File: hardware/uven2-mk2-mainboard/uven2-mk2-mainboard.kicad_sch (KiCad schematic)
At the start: 126 parts, among them J1 LEDs, J10 GND, J11 24V, J12 GND, J13 24V, J14 GND, J15 Chamber_Control, J17 PowerON/OFF, J2 1-282834-0, J3 5V, J4 GND, J5 J1B1211CCD, J6 24V, J7 GND, J8 USB_HOST, J9 24V, Q1 2N7002, Q2 2N7002, U1 DEV-16771, U2 MCP48FEB28T-20E/ST, U3 MCP48FEB28T-20E/ST

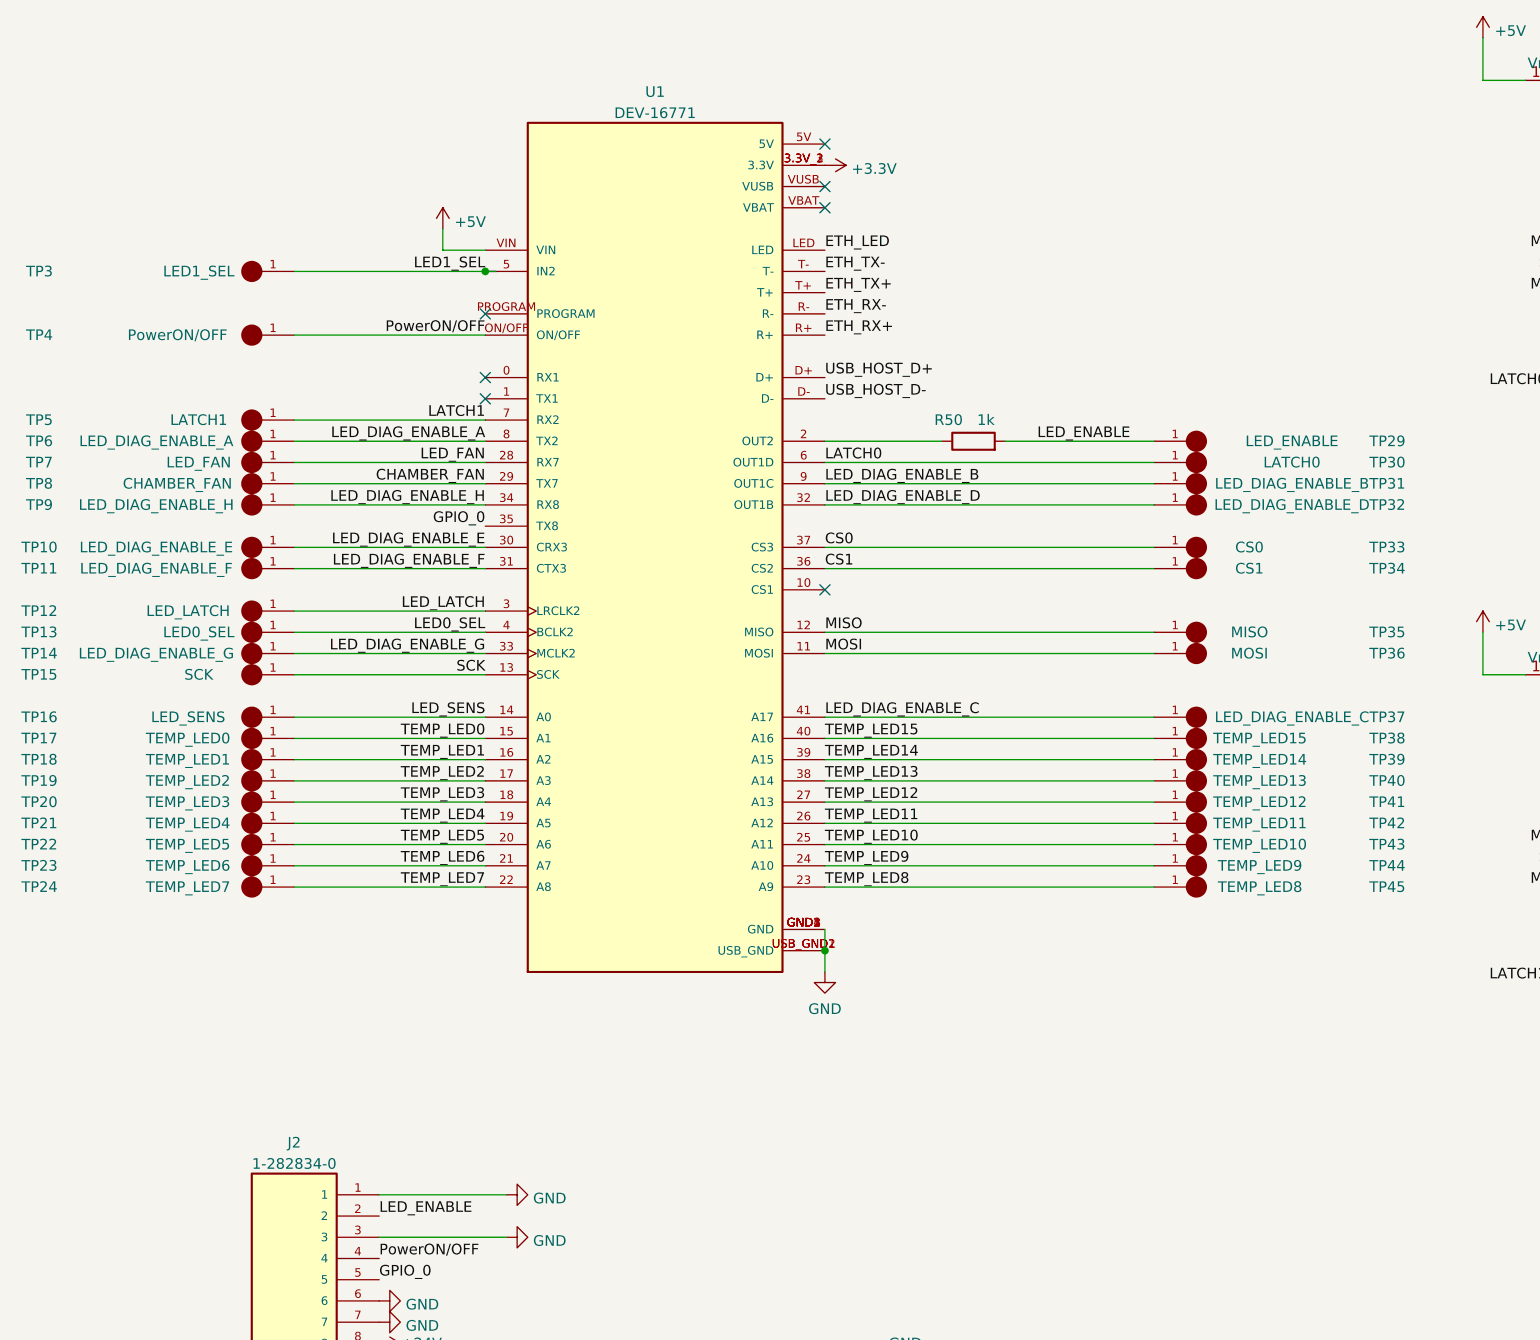
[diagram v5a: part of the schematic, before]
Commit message: layout led driver almost done
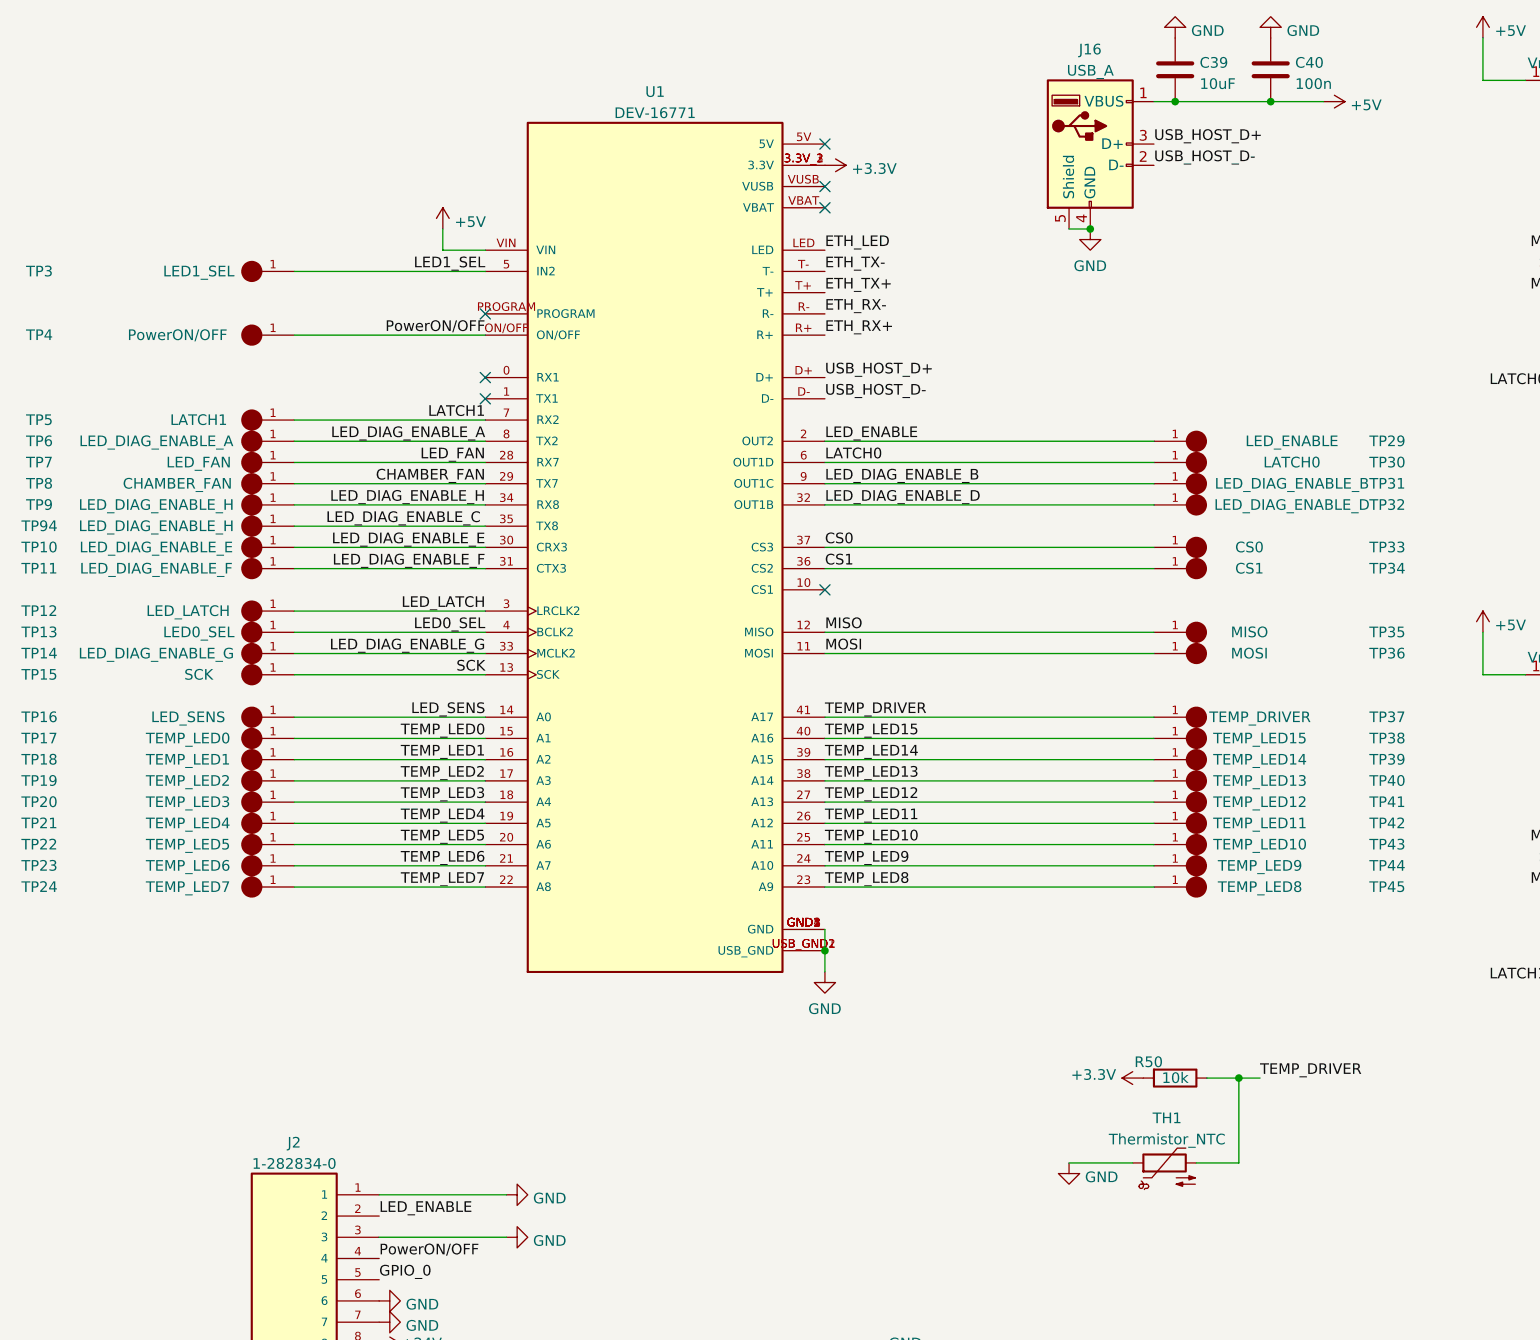
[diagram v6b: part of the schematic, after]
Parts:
- removed R50: 1k, Resistor_SMD:R_0603_1608Metric_Pad0.98x0.95mm_HandSolder, symbol Device:R
- added C39: 10uF, Capacitor_SMD:C_0603_1608Metric_Pad1.08x0.95mm_HandSolder, symbol Device:C
- added C40: 100n, Capacitor_SMD:C_0603_1608Metric_Pad1.08x0.95mm_HandSolder, symbol Device:C
- added J16: USB_A, Connector_USB:USB_A_Molex_67643_Horizontal, symbol Connector:USB_A
- added R50: 10k, Resistor_SMD:R_0603_1608Metric_Pad0.98x0.95mm_HandSolder, symbol uven-mainboard-rescue:R-Device
- added TH1: Thermistor_NTC, Resistor_SMD:R_0805_2012Metric_Pad1.20x1.40mm_HandSolder, symbol Device:Thermistor_NTC
- added TP94: LED_DIAG_ENABLE_H, custom_lib:TP420X150, symbol RCWCTE:RCWCTE
- TP37: value LED_DIAG_ENABLE_C -> TEMP_DRIVER
- TP62, TP63, TP64, TP65, TP66, TP67, TP68, TP69, TP70, TP71, TP72, TP73, TP74, TP75, TP76, TP77, TP78, TP79, TP80, TP81, TP82, TP83, TP84, TP85, TP86, TP87, TP88, TP89, TP90, TP91, TP92, TP93: footprint custom_lib:TP420X150 -> TestPoint:TestPoint_THTPad_1.0x1.0mm_Drill0.5mm
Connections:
- net +5V: now also C39.2, C40.2, J16.1 (VBUS)
- net GND: now also C39.1, C40.1, J16.4 (GND), J16.5 (Shield), TH1.1
- net GPIO_0: no longer U1.35 (TX8)
- net LED_DIAG_ENABLE_C: now also U1.35 (TX8), TP94.1; no longer TP37.1, U1.41 (A17)
- net LED_ENABLE: now also U1.2 (OUT2)
- net USB_HOST_D+: now also J16.3 (D+)
- net USB_HOST_D-: now also J16.2 (D-)
- new net +3V3: R50.2
- new net TEMP_DRIVER: R50.1, TH1.2, TP37.1, U1.41 (A17)

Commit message: layout almost finished
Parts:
- removed JP2: Vref_select, Jumper:SolderJumper-3_P1.3mm_Open_RoundedPad1.0x1.5mm_NumberLabels, symbol Jumper:SolderJumper_3_Open
- removed TP62: LED15+, TestPoint:TestPoint_THTPad_1.0x1.0mm_Drill0.5mm, symbol RCWCTE:RCWCTE
- removed TP63: LED15-, TestPoint:TestPoint_THTPad_1.0x1.0mm_Drill0.5mm, symbol RCWCTE:RCWCTE
- removed TP64: LED14+, TestPoint:TestPoint_THTPad_1.0x1.0mm_Drill0.5mm, symbol RCWCTE:RCWCTE
- removed TP65: LED14-, TestPoint:TestPoint_THTPad_1.0x1.0mm_Drill0.5mm, symbol RCWCTE:RCWCTE
- removed TP66: LED13+, TestPoint:TestPoint_THTPad_1.0x1.0mm_Drill0.5mm, symbol RCWCTE:RCWCTE
- removed TP67: LED13-, TestPoint:TestPoint_THTPad_1.0x1.0mm_Drill0.5mm, symbol RCWCTE:RCWCTE
- removed TP68: LED12+, TestPoint:TestPoint_THTPad_1.0x1.0mm_Drill0.5mm, symbol RCWCTE:RCWCTE
- removed TP69: LED12-, TestPoint:TestPoint_THTPad_1.0x1.0mm_Drill0.5mm, symbol RCWCTE:RCWCTE
- removed TP70: LED11+, TestPoint:TestPoint_THTPad_1.0x1.0mm_Drill0.5mm, symbol RCWCTE:RCWCTE
- removed TP71: LED11-, TestPoint:TestPoint_THTPad_1.0x1.0mm_Drill0.5mm, symbol RCWCTE:RCWCTE
- removed TP72: LED10+, TestPoint:TestPoint_THTPad_1.0x1.0mm_Drill0.5mm, symbol RCWCTE:RCWCTE
- removed TP73: LED10-, TestPoint:TestPoint_THTPad_1.0x1.0mm_Drill0.5mm, symbol RCWCTE:RCWCTE
- removed TP74: LED9+, TestPoint:TestPoint_THTPad_1.0x1.0mm_Drill0.5mm, symbol RCWCTE:RCWCTE
- removed TP75: LED9-, TestPoint:TestPoint_THTPad_1.0x1.0mm_Drill0.5mm, symbol RCWCTE:RCWCTE
- removed TP76: LED8+, TestPoint:TestPoint_THTPad_1.0x1.0mm_Drill0.5mm, symbol RCWCTE:RCWCTE
- removed TP77: LED8-, TestPoint:TestPoint_THTPad_1.0x1.0mm_Drill0.5mm, symbol RCWCTE:RCWCTE
- removed TP78: LED7+, TestPoint:TestPoint_THTPad_1.0x1.0mm_Drill0.5mm, symbol RCWCTE:RCWCTE
- removed TP79: LED7-, TestPoint:TestPoint_THTPad_1.0x1.0mm_Drill0.5mm, symbol RCWCTE:RCWCTE
- removed TP80: LED6+, TestPoint:TestPoint_THTPad_1.0x1.0mm_Drill0.5mm, symbol RCWCTE:RCWCTE
- removed TP81: LED6-, TestPoint:TestPoint_THTPad_1.0x1.0mm_Drill0.5mm, symbol RCWCTE:RCWCTE
- removed TP82: LED5+, TestPoint:TestPoint_THTPad_1.0x1.0mm_Drill0.5mm, symbol RCWCTE:RCWCTE
- removed TP83: LED5-, TestPoint:TestPoint_THTPad_1.0x1.0mm_Drill0.5mm, symbol RCWCTE:RCWCTE
- removed TP84: LED4+, TestPoint:TestPoint_THTPad_1.0x1.0mm_Drill0.5mm, symbol RCWCTE:RCWCTE
- removed TP85: LED4-, TestPoint:TestPoint_THTPad_1.0x1.0mm_Drill0.5mm, symbol RCWCTE:RCWCTE
- removed TP86: LED3+, TestPoint:TestPoint_THTPad_1.0x1.0mm_Drill0.5mm, symbol RCWCTE:RCWCTE
- removed TP87: LED3-, TestPoint:TestPoint_THTPad_1.0x1.0mm_Drill0.5mm, symbol RCWCTE:RCWCTE
- removed TP88: LED2+, TestPoint:TestPoint_THTPad_1.0x1.0mm_Drill0.5mm, symbol RCWCTE:RCWCTE
- removed TP89: LED2-, TestPoint:TestPoint_THTPad_1.0x1.0mm_Drill0.5mm, symbol RCWCTE:RCWCTE
- removed TP90: LED1+, TestPoint:TestPoint_THTPad_1.0x1.0mm_Drill0.5mm, symbol RCWCTE:RCWCTE
- removed TP91: LED1-, TestPoint:TestPoint_THTPad_1.0x1.0mm_Drill0.5mm, symbol RCWCTE:RCWCTE
- removed TP92: LED0+, TestPoint:TestPoint_THTPad_1.0x1.0mm_Drill0.5mm, symbol RCWCTE:RCWCTE
- removed TP93: LED0-, TestPoint:TestPoint_THTPad_1.0x1.0mm_Drill0.5mm, symbol RCWCTE:RCWCTE
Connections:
- net TEMP_LED0: now also J15.9; no longer J15.1
- net TEMP_LED1: now also J15.8; no longer J15.2
- net TEMP_LED13: now also J15.16; no longer J15.14
- net TEMP_LED15: now also J15.14; no longer J15.16
- net TEMP_LED2: now also J15.7; no longer J15.3
- net TEMP_LED3: now also J15.6; no longer J15.4
- net TEMP_LED5: now also J15.4; no longer J15.6
- net TEMP_LED6: now also J15.3; no longer J15.7
- net TEMP_LED7: now also J15.2; no longer J15.8
- net TEMP_LED8: now also J15.1; no longer J15.9
- net at U3.16 (VREF1), U3.4 (VREF0): now also JP1.2 (C), U2.16 (VREF1), U2.4 (VREF0)

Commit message: layout finished
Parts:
- added H1, H2, H3, H4, H5: MountingHole, MountingHole:MountingHole_3.2mm_M3, symbol Mechanical:MountingHole
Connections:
- net GPIO_0 is gone; now on net GND: J2.5
- net +3.3V: now also J2.6
- net GND: no longer J2.6
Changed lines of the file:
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@@
     (effects (font (size 1.27 1.27)) (justify left bottom))
   )
-  (label "GPIO_0" (at 55.88 168.91 0)
-    (effects (font (size 1.27 1.27)) (justify left bottom))
-  )
   (label "LED_SENS" (at 328.93 104.14 0)
     (effects (font (size 1.27 1.27)) (justify left bottom))
@@
     (pin "1")
   )
+  (symbol (lib_id "Mechanical:MountingHole") (at 314.96 167.64 0) (unit 1)
+    (in_bom yes) (on_board yes) (fields_autoplaced)
+    (property "Reference" "H2" (id 0) (at 317.5 166.8053 0)
+      (effects (font (size 1.27 1.27)) (justify left))
+    )
+    (property "Value" "MountingHole" (id 1) (at 317.5 169.3422 0)
+      (effects (font (size 1.27 1.27)) (justify left))
+    )
+    (property "Footprint" "MountingHole:MountingHole_3.2mm_M3" (id 2) (at 314.96 167.64 0)
+      (effects (font (size 1.27 1.27)) hide)
+    )
+    (property "Datasheet" "~" (id 3) (at 314.96 167.64 0)
+      (effects (font (size 1.27 1.27)) hide)
+    )
+  )
   (symbol (lib_id "RCWCTE:RCWCTE") (at 252.73 120.65 0) (unit 1)
     (in_bom yes) (on_board yes)
@@
     (pin "1")
   )
-  (symbol (lib_id "power:GND") (at 55.88 171.45 90) (unit 1)
+  (symbol (lib_id "power:GND") (at 55.88 168.91 90) (unit 1)
     (in_bom yes) (on_board yes) (fields_autoplaced)
-    (property "Reference" "#PWR0230" (id 0) (at 62.23 171.45 0)
+    (property "Reference" "#PWR0230" (id 0) (at 62.23 168.91 0)
       (effects (font (size 1.27 1.27)) hide)
     )
-    (property "Value" "GND" (id 1) (at 59.055 171.8838 90)
+    (property "Value" "GND" (id 1) (at 59.055 169.3438 90)
       (effects (font (size 1.27 1.27)) (justify right))
     )
-    (property "Footprint" "" (id 2) (at 55.88 171.45 0)
+    (property "Footprint" "" (id 2) (at 55.88 168.91 0)
       (effects (font (size 1.27 1.27)) hide)
     )
-    (property "Datasheet" "" (id 3) (at 55.88 171.45 0)
+    (property "Datasheet" "" (id 3) (at 55.88 168.91 0)
       (effects (font (size 1.27 1.27)) hide)
     )
@@
     (pin "1")
   )
+  (symbol (lib_id "Mechanical:MountingHole") (at 314.96 175.26 0) (unit 1)
+    (in_bom yes) (on_board yes) (fields_autoplaced)
+    (property "Reference" "H3" (id 0) (at 317.5 174.4253 0)
+      (effects (font (size 1.27 1.27)) (justify left))
+    )
+    (property "Value" "MountingHole" (id 1) (at 317.5 176.9622 0)
+      (effects (font (size 1.27 1.27)) (justify left))
+    )
+    (property "Footprint" "MountingHole:MountingHole_3.2mm_M3" (id 2) (at 314.96 175.26 0)
+      (effects (font (size 1.27 1.27)) hide)
+    )
+    (property "Datasheet" "~" (id 3) (at 314.96 175.26 0)
+      (effects (font (size 1.27 1.27)) hide)
+    )
+  )
   (symbol (lib_id "RCWCTE:RCWCTE") (at 40.64 101.6 180) (unit 1)
     (in_bom yes) (on_board yes)
@@
     (pin "1")
   )
+  (symbol (lib_id "power:+3.3V") (at 55.88 171.45 270) (unit 1)
+    (in_bom yes) (on_board yes) (fields_autoplaced)
+    (property "Reference" "#PWR?" (id 0) (at 52.07 171.45 0)
+      (effects (font (size 1.27 1.27)) hide)
+    )
+    (property "Value" "+3.3V" (id 1) (at 59.055 171.8838 90)
+      (effects (font (size 1.27 1.27)) (justify left))
+    )
+    (property "Footprint" "" (id 2) (at 55.88 171.45 0)
+      (effects (font (size 1.27 1.27)) hide)
+    )
+    (property "Datasheet" "" (id 3) (at 55.88 171.45 0)
+      (effects (font (size 1.27 1.27)) hide)
+    )
+    (pin "1")
+  )
   (symbol (lib_id "Connector:Conn_01x01_Female") (at 167.64 208.28 0) (unit 1)
     (in_bom yes) (on_board yes) (fields_autoplaced)
@@
     (pin "1")
   )
+  (symbol (lib_id "Mechanical:MountingHole") (at 314.96 190.5 0) (unit 1)
+    (in_bom yes) (on_board yes) (fields_autoplaced)
+    (property "Reference" "H5" (id 0) (at 317.5 189.6653 0)
+      (effects (font (size 1.27 1.27)) (justify left))
+    )
+    (property "Value" "MountingHole" (id 1) (at 317.5 192.2022 0)
+      (effects (font (size 1.27 1.27)) (justify left))
+    )
+    (property "Footprint" "MountingHole:MountingHole_3.2mm_M3" (id 2) (at 314.96 190.5 0)
+      (effects (font (size 1.27 1.27)) hide)
+    )
+    (property "Datasheet" "~" (id 3) (at 314.96 190.5 0)
+      (effects (font (size 1.27 1.27)) hide)
+    )
+  )
   (symbol (lib_id "power:GND") (at 248.92 243.84 90) (unit 1)
     (in_bom yes) (on_board yes)
@@
     (pin "1")
   )
+  (symbol (lib_id "Mechanical:MountingHole") (at 314.96 182.88 0) (unit 1)
+    (in_bom yes) (on_board yes) (fields_autoplaced)
+    (property "Reference" "H4" (id 0) (at 317.5 182.0453 0)
+      (effects (font (size 1.27 1.27)) (justify left))
+    )
+    (property "Value" "MountingHole" (id 1) (at 317.5 184.5822 0)
+      (effects (font (size 1.27 1.27)) (justify left))
+    )
+    (property "Footprint" "MountingHole:MountingHole_3.2mm_M3" (id 2) (at 314.96 182.88 0)
+      (effects (font (size 1.27 1.27)) hide)
+    )
+    (property "Datasheet" "~" (id 3) (at 314.96 182.88 0)
+      (effects (font (size 1.27 1.27)) hide)
+    )
+  )
   (symbol (lib_id "power:GND") (at 146.05 219.71 0) (unit 1)
     (in_bom yes) (on_board yes) (fields_autoplaced)
@@
     (pin "1")
   )
+  (symbol (lib_id "Mechanical:MountingHole") (at 314.96 160.02 0) (unit 1)
+    (in_bom yes) (on_board yes) (fields_autoplaced)
+    (property "Reference" "H1" (id 0) (at 317.5 159.1853 0)
+      (effects (font (size 1.27 1.27)) (justify left))
+    )
+    (property "Value" "MountingHole" (id 1) (at 317.5 161.7222 0)
+      (effects (font (size 1.27 1.27)) (justify left))
+    )
+    (property "Footprint" "MountingHole:MountingHole_3.2mm_M3" (id 2) (at 314.96 160.02 0)
+      (effects (font (size 1.27 1.27)) hide)
+    )
+    (property "Datasheet" "~" (id 3) (at 314.96 160.02 0)
+      (effects (font (size 1.27 1.27)) hide)
+    )
+  )
   (sheet (at 360.68 53.34) (size 24.13 20.32) (fields_autoplaced)
     (stroke (width 0.1524) (type solid) (color 0 0 0 0))
@@
       (reference "#PWR0261") (unit 1) (value "GND") (footprint "")
     )
+    (path "/8f15e43a-f43b-4fe7-a252-39f2b26b193d"
+      (reference "#PWR?") (unit 1) (value "+3.3V") (footprint "")
+    )
     (path "/74394a4e-e68c-4574-bde0-dd3ca18d2b15"
       (reference "C1") (unit 1) (value "100n") (footprint "Capacitor_SMD:C_0603_1608Metric_Pad1.08x0.95mm_HandSolder")
@@
       (reference "C40") (unit 1) (value "100n") (footprint "Capacitor_SMD:C_0603_1608Metric_Pad1.08x0.95mm_HandSolder")
     )
+    (path "/fd53414d-fed1-4192-a4a6-6e71719f5ee3"
+      (reference "H1") (unit 1) (value "MountingHole") (footprint "MountingHole:MountingHole_3.2mm_M3")
+    )
+    (path "/00f586cb-2154-4f57-8536-a80ccefa541b"
+      (reference "H2") (unit 1) (value "MountingHole") (footprint "MountingHole:MountingHole_3.2mm_M3")
+    )
+    (path "/748d5c83-47c0-4e03-ae8e-d5c13f637577"
+      (reference "H3") (unit 1) (value "MountingHole") (footprint "MountingHole:MountingHole_3.2mm_M3")
+    )
+    (path "/cadacbd8-9e6a-4a95-b64f-c3a322eedc7e"
+      (reference "H4") (unit 1) (value "MountingHole") (footprint "MountingHole:MountingHole_3.2mm_M3")
+    )
+    (path "/b52d3deb-82f4-410a-8236-79b6b7fb704f"
+      (reference "H5") (unit 1) (value "MountingHole") (footprint "MountingHole:MountingHole_3.2mm_M3")
+    )
     (path "/87d3aefe-ec7f-48f1-b85f-4e077bd5ef04"
